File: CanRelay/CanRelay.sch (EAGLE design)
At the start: 22 parts

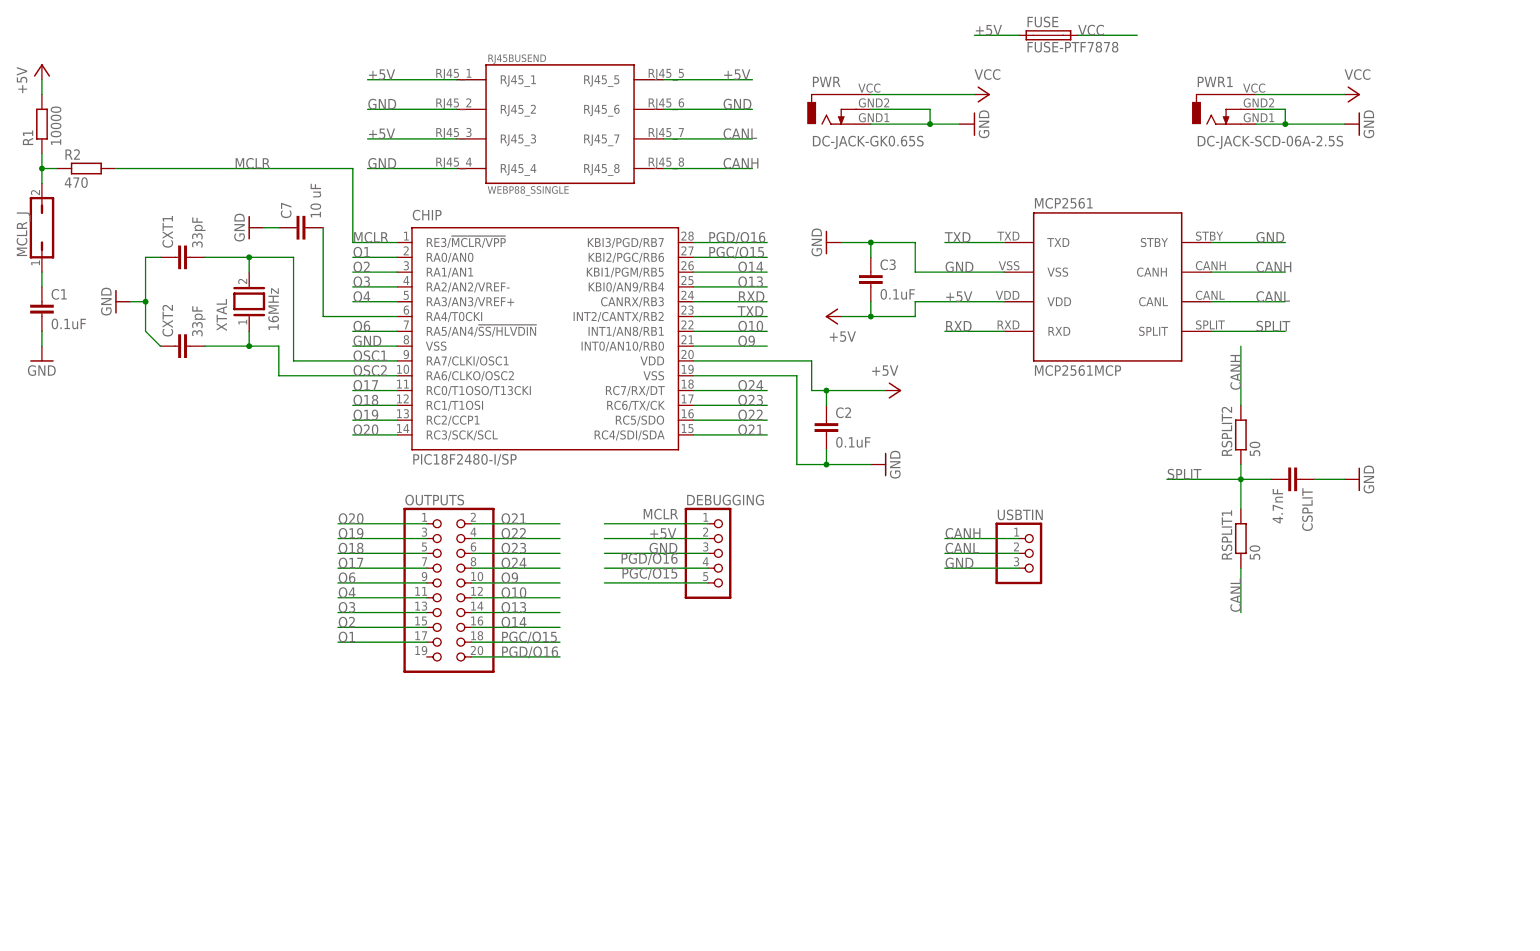
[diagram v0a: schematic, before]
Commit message: #19 dropped old chip, put new chip from eagle library on the schematic. put all mandatory connections to the chip so far only, so one more capacitor since this variant has 2 pairs of VSS and VDD pins, put all to schema, including MCLR, voltage reg, input power, crystal pins. Schema is therefore done for all but outputs. Board half way through
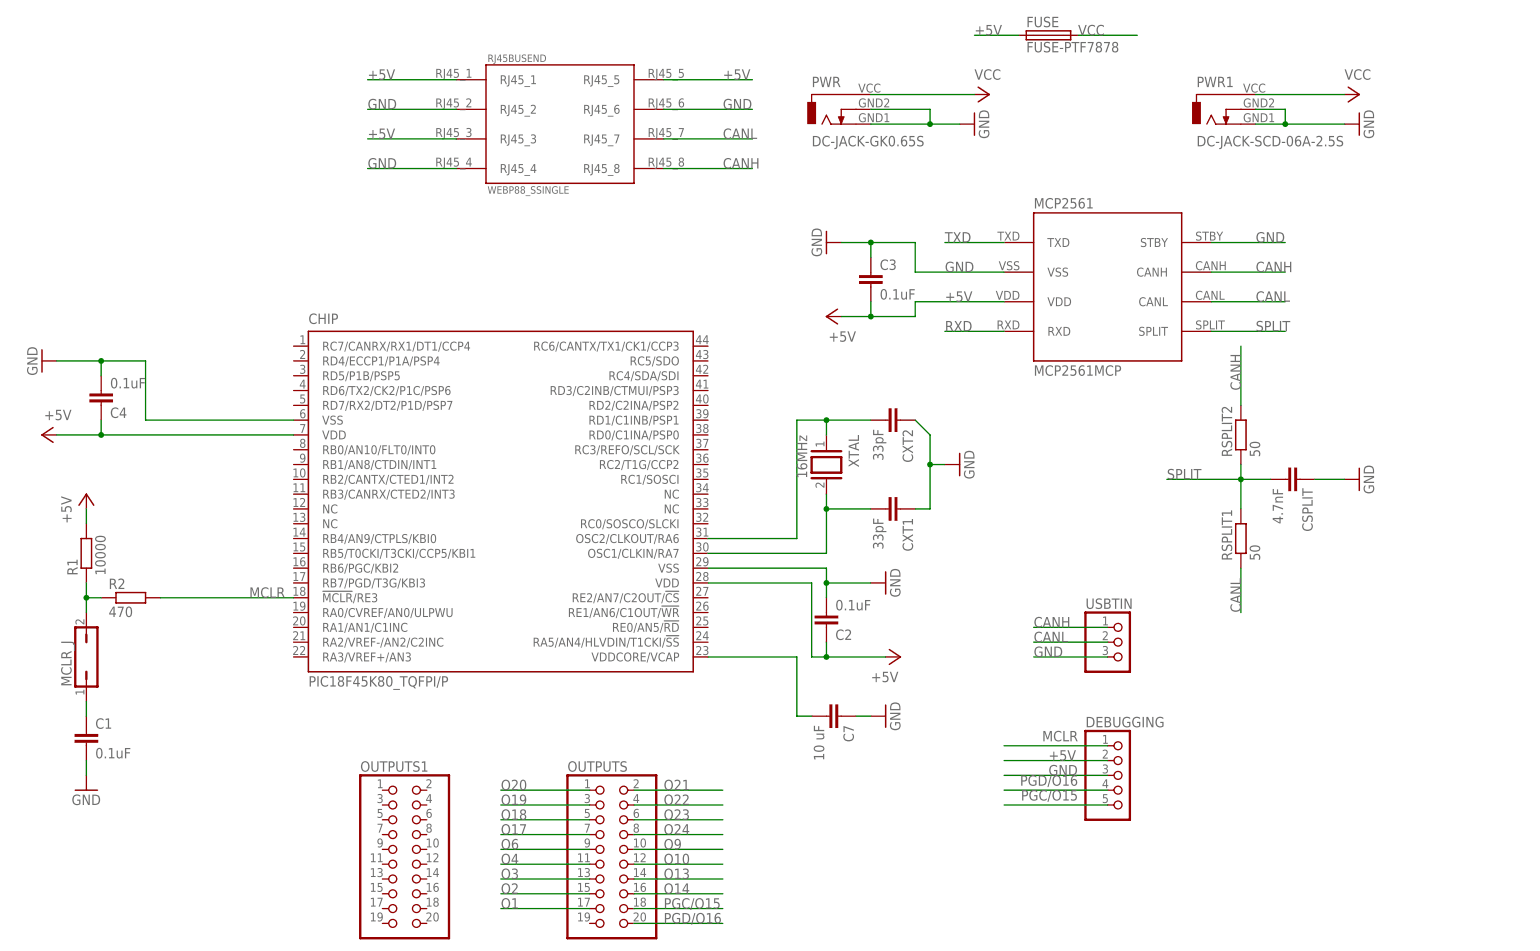
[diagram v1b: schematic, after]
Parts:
- added C4: 0.1uF, rcl:C-EU050-025X075
- added OUTPUTS1: (no value), pinhead:PINHD-2X10
- CHIP: value PIC18F2480-I/SP -> PIC18F45K80_TQFPI/P; device microchip:PIC18F2480-I/SP -> PoJD:PIC18F45K80_TQFPI/P
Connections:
- net +5V: now also C4.1, CHIP.VDD@1
- net GND: now also C4.2
- net MCLR: now also CHIP.!MCLR!/RE3; no longer CHIP.RE3/!MCLR/VPP
- net N$4: now also CHIP.VDDCORE/VCAP; no longer CHIP.RA4/T0CKI
- net O1: no longer CHIP.RA0/AN0
- net O10: no longer CHIP.INT1/AN8/RB1
- net O13: no longer CHIP.KBI0/AN9/RB4
- net O14: no longer CHIP.KBI1/PGM/RB5
- net O17: no longer CHIP.RC0/T1OSO/T13CKI
- net O18: no longer CHIP.RC1/T1OSI
- net O19: no longer CHIP.RC2/CCP1
- net O2: no longer CHIP.RA1/AN1
- net O20: no longer CHIP.RC3/SCK/SCL
- net O21: no longer CHIP.RC4/SDI/SDA
- net O22: no longer CHIP.RC5/SDO
- net O23: no longer CHIP.RC6/TX/CK
- net O24: no longer CHIP.RC7/RX/DT
- net O3: no longer CHIP.RA2/AN2/VREF-
- net O4: no longer CHIP.RA3/AN3/VREF+
- net O6: no longer CHIP.RA5/AN4/!SS/HLVDIN
- net O9: no longer CHIP.INT0/AN10/RB0
- net OSC1: now also CHIP.OSC1/CLKIN/RA7; no longer CHIP.RA7/CLKI/OSC1
- net OSC2: now also CHIP.OSC2/CLKOUT/RA6; no longer CHIP.RA6/CLKO/OSC2
- net PGC/O15: no longer CHIP.KBI2/PGC/RB6
- net PGD/O16: no longer CHIP.KBI3/PGD/RB7
- net RXD: no longer CHIP.CANRX/RB3
- net TXD: no longer CHIP.INT2/CANTX/RB2
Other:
- moved on the sheet: C1, C2, C7, CXT1, CXT2, DEBUGGING, MCLR_J, OUTPUTS, R1, R2, USBTIN, XTAL

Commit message: #19 connected all but output ports, including RXD and TXD on both schema and the board, with no erc errors. Rotated the chip in the end to get MCLR and programming up and RX and TX closer to the transceiver. all seems sort of OKish so far, missing all outputs which are likely to mess things up
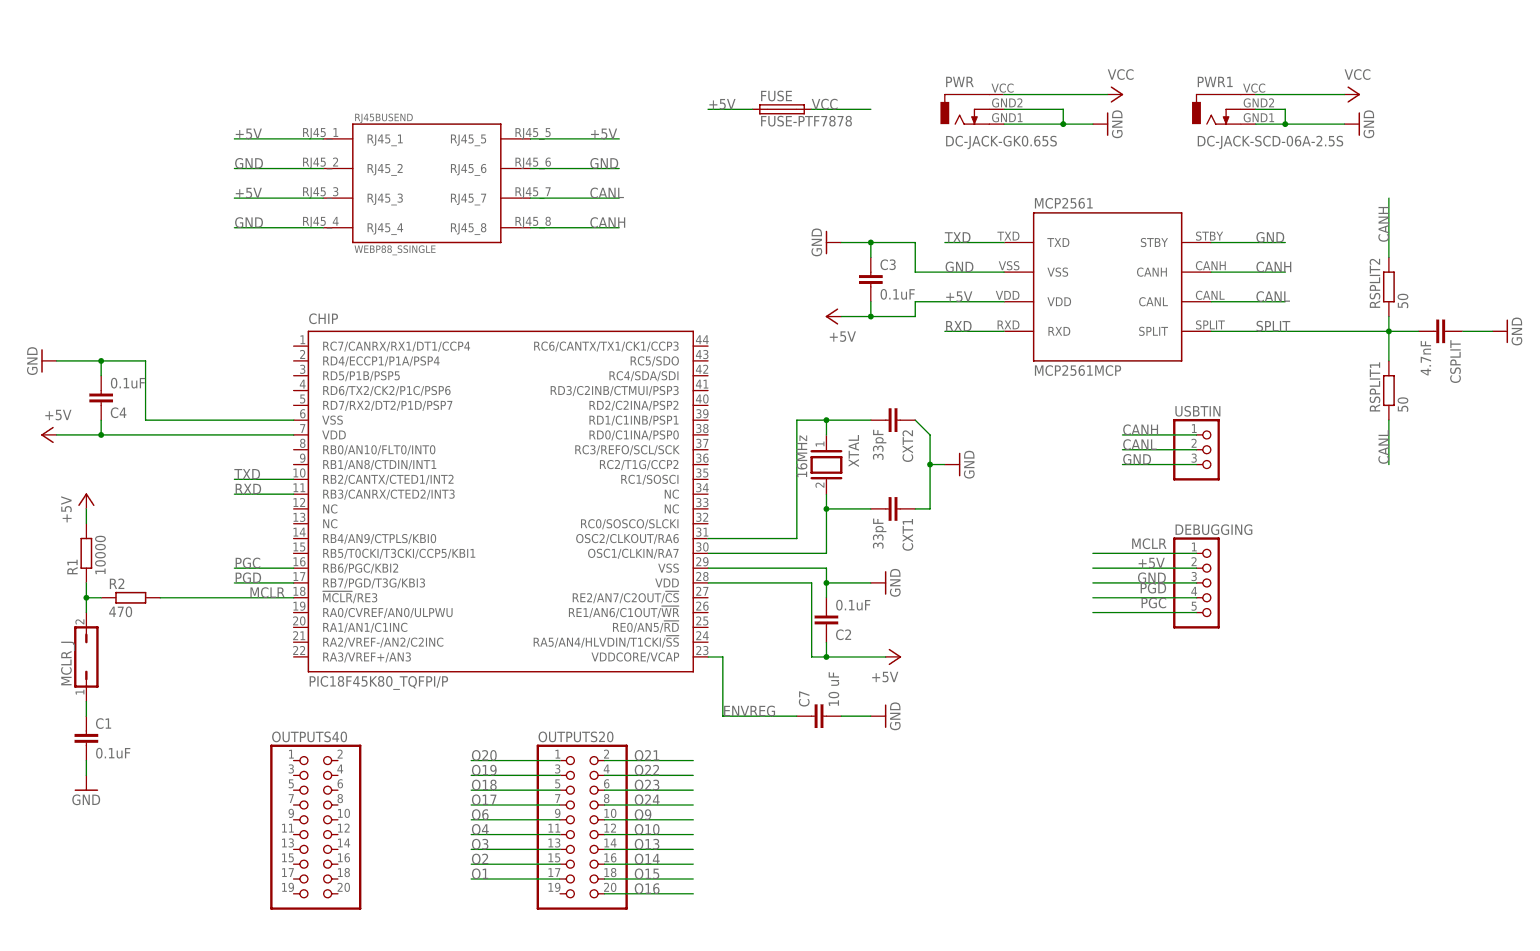
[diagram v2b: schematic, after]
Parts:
- removed OUTPUTS, OUTPUTS1: (no value), pinhead:PINHD-2X10
- added OUTPUTS20, OUTPUTS40: (no value), pinhead:PINHD-2X10
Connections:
- removed net N$4: C7.2, CHIP.VDDCORE/VCAP
- removed net PGC/O15: DEBUGGING.5, OUTPUTS.18
- removed net PGD/O16: DEBUGGING.4, OUTPUTS.20
- new net ENVREG: C7.1, CHIP.VDDCORE/VCAP
- new net O15: OUTPUTS20.18
- new net O16: OUTPUTS20.20
- new net PGC: CHIP.RB6/PGC/KBI2, DEBUGGING.5
- new net PGD: CHIP.RB7/PGD/T3G/KBI3, DEBUGGING.4
- net GND: now also C7.2; no longer C7.1
- net O1: now also OUTPUTS20.17; no longer OUTPUTS.17
- net O10: now also OUTPUTS20.12; no longer OUTPUTS.12
- net O13: now also OUTPUTS20.14; no longer OUTPUTS.14
- net O14: now also OUTPUTS20.16; no longer OUTPUTS.16
- net O17: now also OUTPUTS20.7; no longer OUTPUTS.7
- net O18: now also OUTPUTS20.5; no longer OUTPUTS.5
- net O19: now also OUTPUTS20.3; no longer OUTPUTS.3
- net O2: now also OUTPUTS20.15; no longer OUTPUTS.15
- net O20: now also OUTPUTS20.1; no longer OUTPUTS.1
- net O21: now also OUTPUTS20.2; no longer OUTPUTS.2
- net O22: now also OUTPUTS20.4; no longer OUTPUTS.4
- net O23: now also OUTPUTS20.6; no longer OUTPUTS.6
- net O24: now also OUTPUTS20.8; no longer OUTPUTS.8
- net O3: now also OUTPUTS20.13; no longer OUTPUTS.13
- net O4: now also OUTPUTS20.11; no longer OUTPUTS.11
- net O6: now also OUTPUTS20.9; no longer OUTPUTS.9
- net O9: now also OUTPUTS20.10; no longer OUTPUTS.10
- net RXD: now also CHIP.RB3/CANRX/CTED2/INT3
- net TXD: now also CHIP.RB2/CANTX/CTED1/INT2
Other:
- moved on the sheet: C7, CSPLIT, DEBUGGING, FUSE, PWR, RJ45BUSEND, RSPLIT1, RSPLIT2, USBTIN

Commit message: #19 started connecting output ports. Bottom pat all done, also labeled properly, moved the whole PCB a few mms up to make space for routes there
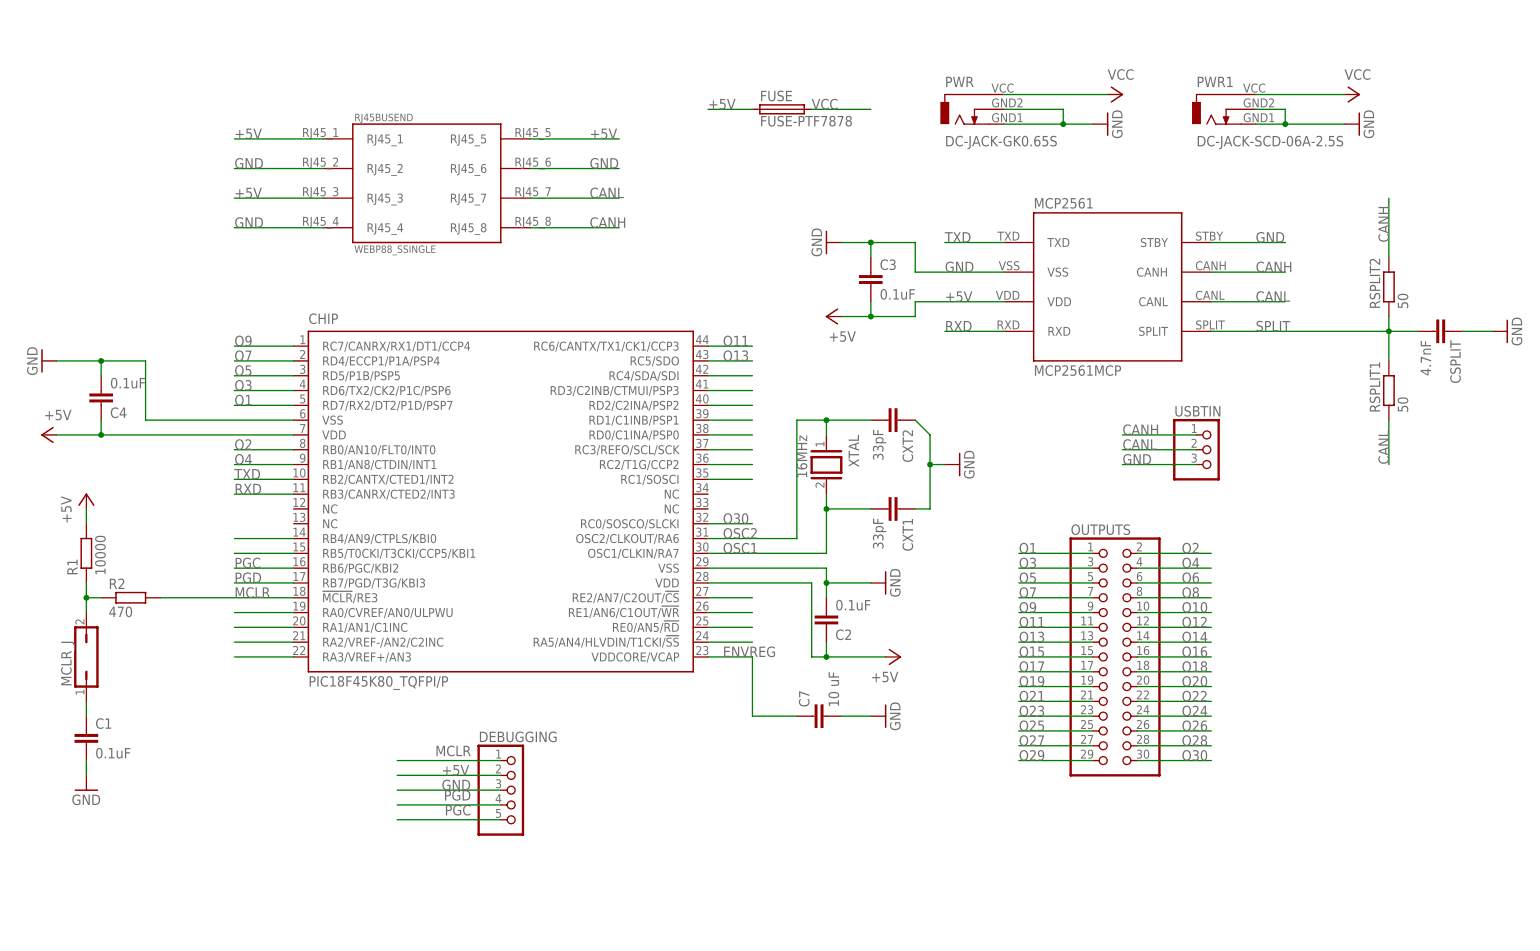
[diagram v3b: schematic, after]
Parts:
- removed OUTPUTS20, OUTPUTS40: (no value), pinhead:PINHD-2X10
- added OUTPUTS: (no value), pinhead:PINHD-2X15
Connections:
- new net N$10: CHIP.RB4/AN9/CTPLS/KBI0
- new net N$11: CHIP.RB5/T0CKI/T3CKI/CCP5/KBI1
- new net N$12: CHIP.RA0/CVREF/AN0/ULPWU
- new net N$13: CHIP.RA1/AN1/C1INC
- new net N$14: CHIP.RA2/VREF-/AN2/C2INC
- new net N$15: CHIP.RA3/VREF+/AN3
- new net N$25: CHIP.RE2/AN7/C2OUT/!CS!
- new net N$26: CHIP.RE1/AN6/C1OUT/!WR!
- new net N$27: CHIP.RE0/AN5/!RD!
- new net N$28: CHIP.RA5/AN4/HLVDIN/T1CKI/!SS!
- new net O11: CHIP.RC6/CANTX/TX1/CK1/CCP3, OUTPUTS.11
- new net O12: OUTPUTS.12
- new net O25: CHIP.RC3/REFO/SCL/SCK, OUTPUTS.25
- new net O26: OUTPUTS.26
- new net O27: CHIP.RC2/T1G/CCP2, OUTPUTS.27
- new net O28: OUTPUTS.28
- new net O29: CHIP.RC1/SOSCI, OUTPUTS.29
- new net O30: CHIP.RC0/SOSCO/SLCKI, OUTPUTS.30
- new net O5: CHIP.RD5/P1B/PSP5, OUTPUTS.5
- new net O7: CHIP.RD4/ECCP1/P1A/PSP4, OUTPUTS.7
- new net O8: OUTPUTS.8
- net O1: now also CHIP.RD7/RX2/DT2/P1D/PSP7, OUTPUTS.1; no longer OUTPUTS20.17
- net O10: now also OUTPUTS.10; no longer OUTPUTS20.12
- net O13: now also CHIP.RC5/SDO, OUTPUTS.13; no longer OUTPUTS20.14
- net O14: now also OUTPUTS.14; no longer OUTPUTS20.16
- net O15: now also CHIP.RC4/SDA/SDI, OUTPUTS.15; no longer OUTPUTS20.18
- net O16: now also OUTPUTS.16; no longer OUTPUTS20.20
- net O17: now also CHIP.RD3/C2INB/CTMUI/PSP3, OUTPUTS.17; no longer OUTPUTS20.7
- net O18: now also OUTPUTS.18; no longer OUTPUTS20.5
- net O19: now also CHIP.RD2/C2INA/PSP2, OUTPUTS.19; no longer OUTPUTS20.3
- net O2: now also CHIP.RB0/AN10/FLT0/INT0, OUTPUTS.2; no longer OUTPUTS20.15
- net O20: now also OUTPUTS.20; no longer OUTPUTS20.1
- net O21: now also CHIP.RD1/C1INB/PSP1, OUTPUTS.21; no longer OUTPUTS20.2
- net O22: now also OUTPUTS.22; no longer OUTPUTS20.4
- net O23: now also CHIP.RD0/C1INA/PSP0, OUTPUTS.23; no longer OUTPUTS20.6
- net O24: now also OUTPUTS.24; no longer OUTPUTS20.8
- net O3: now also CHIP.RD6/TX2/CK2/P1C/PSP6, OUTPUTS.3; no longer OUTPUTS20.13
- net O4: now also CHIP.RB1/AN8/CTDIN/INT1, OUTPUTS.4; no longer OUTPUTS20.11
- net O6: now also OUTPUTS.6; no longer OUTPUTS20.9
- net O9: now also CHIP.RC7/CANRX/RX1/DT1/CCP4, OUTPUTS.9; no longer OUTPUTS20.10
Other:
- moved on the sheet: DEBUGGING

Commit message: #19 wired all up. Rewired bottom part a bit too to avoid clearance errors, rather more space down there. Also rewired +5V a bit close to MCLR resistor. Also routed RXD and TXD and PGC and PGD and chose the most feasible outputs to wire them up to. Ran DRC and error checks, all fine now. Missing checking all, adding labels
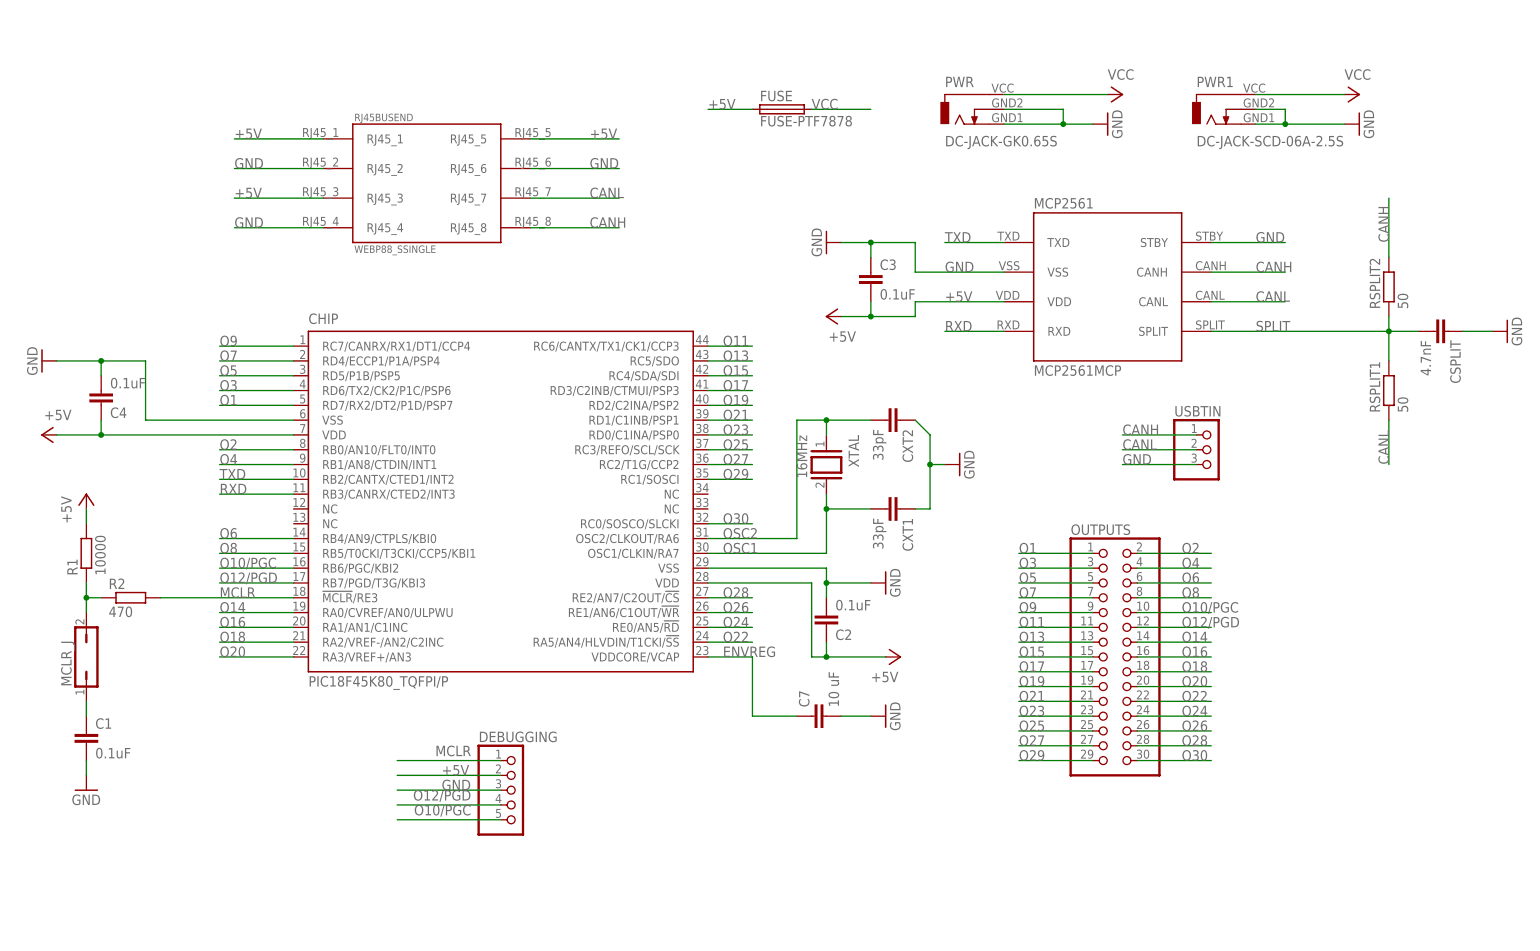
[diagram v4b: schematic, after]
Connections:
- removed net N$10: CHIP.RB4/AN9/CTPLS/KBI0
- removed net N$11: CHIP.RB5/T0CKI/T3CKI/CCP5/KBI1
- removed net N$12: CHIP.RA0/CVREF/AN0/ULPWU
- removed net N$13: CHIP.RA1/AN1/C1INC
- removed net N$14: CHIP.RA2/VREF-/AN2/C2INC
- removed net N$15: CHIP.RA3/VREF+/AN3
- removed net N$25: CHIP.RE2/AN7/C2OUT/!CS!
- removed net N$26: CHIP.RE1/AN6/C1OUT/!WR!
- removed net N$27: CHIP.RE0/AN5/!RD!
- removed net N$28: CHIP.RA5/AN4/HLVDIN/T1CKI/!SS!
- removed net O10: OUTPUTS.10
- removed net O12: OUTPUTS.12
- removed net PGC: CHIP.RB6/PGC/KBI2, DEBUGGING.5
- removed net PGD: CHIP.RB7/PGD/T3G/KBI3, DEBUGGING.4
- new net O10/PGC: CHIP.RB6/PGC/KBI2, DEBUGGING.5, OUTPUTS.10
- new net O12/PGD: CHIP.RB7/PGD/T3G/KBI3, DEBUGGING.4, OUTPUTS.12
- net O14: now also CHIP.RA0/CVREF/AN0/ULPWU
- net O16: now also CHIP.RA1/AN1/C1INC
- net O18: now also CHIP.RA2/VREF-/AN2/C2INC
- net O20: now also CHIP.RA3/VREF+/AN3
- net O22: now also CHIP.RA5/AN4/HLVDIN/T1CKI/!SS!
- net O24: now also CHIP.RE0/AN5/!RD!
- net O26: now also CHIP.RE1/AN6/C1OUT/!WR!
- net O28: now also CHIP.RE2/AN7/C2OUT/!CS!
- net O6: now also CHIP.RB4/AN9/CTPLS/KBI0
- net O8: now also CHIP.RB5/T0CKI/T3CKI/CCP5/KBI1
